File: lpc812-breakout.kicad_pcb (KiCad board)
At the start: 2 copper layers, 24 x 37.5 mm, 28 parts, among them J1 SWD, J2 Left, J3 Right, Q1 BC847BDW1, SW1 Reset, U1 LPC812M101JDH20, Y1 8MHz

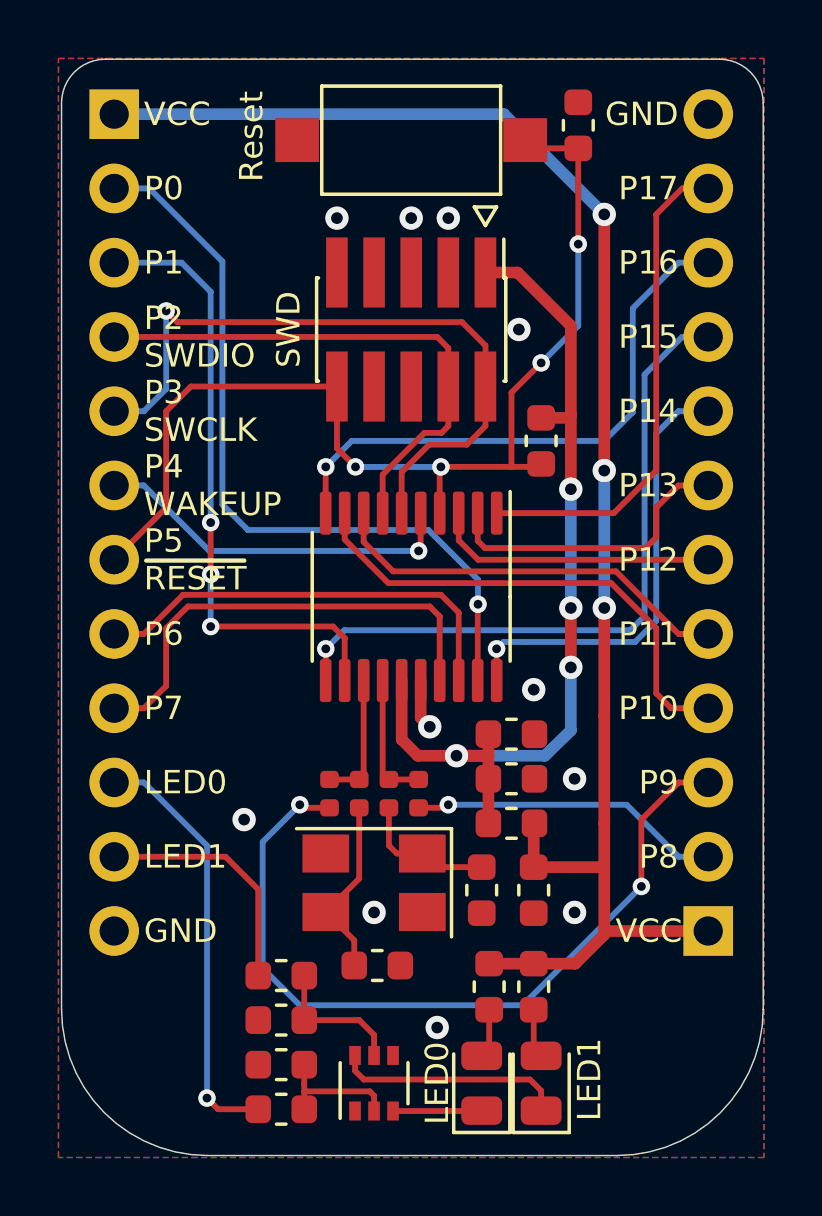
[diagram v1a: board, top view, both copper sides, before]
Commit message: Swapped SWDCLK and SWDIO - D'oh!
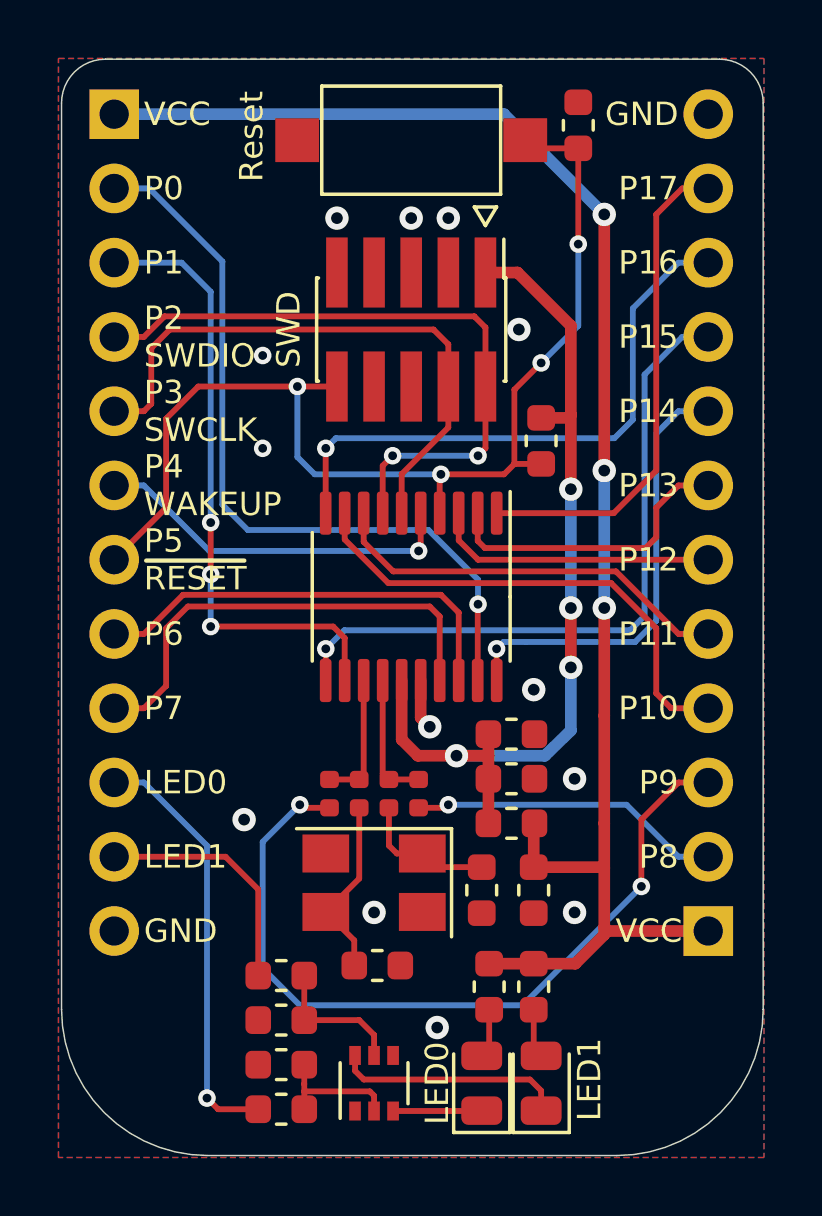
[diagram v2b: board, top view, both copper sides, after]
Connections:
- J1 pad 2: /P3_SWCLK -> /P2_SWDIO
- J1 pad 4: /P2_SWDIO -> /P3_SWCLK
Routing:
- net /P2_SWDIO: track 18.5 -> 22.7 mm, vias 0 -> 2
- net /P3_SWCLK: track 23.8 -> 20.3 mm, vias 1 -> 0
- net /~RESET: track 36.8 -> 38.0 mm
- net /P16: track 19.6 -> 20.2 mm
- net GND: vias 11 -> 13

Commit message: Swapped LED0 with LED1 on the PCB (wrong labels, d'oh!)
Rerouted the Reset and SWD tracks
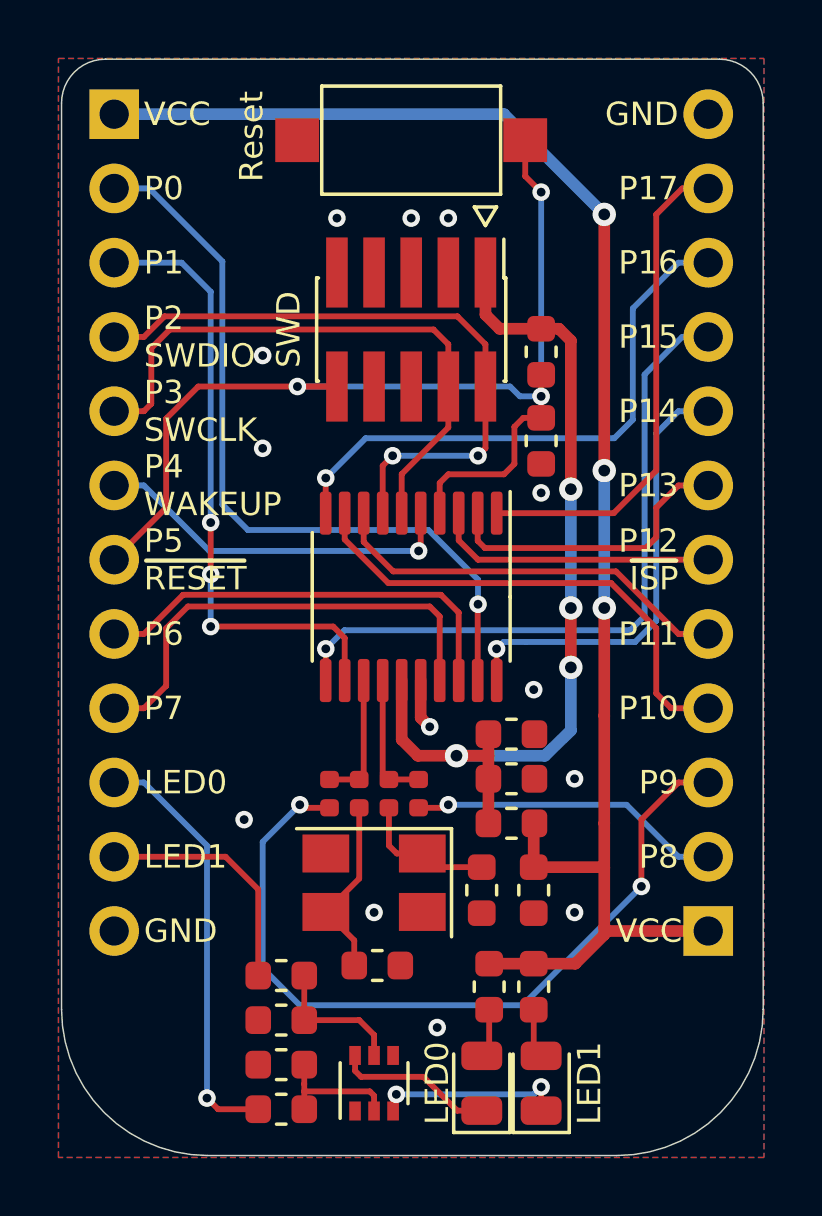
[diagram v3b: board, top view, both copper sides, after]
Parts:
- moved C5 10.9 mm to (141.6, 92.5), turned to 270 degrees
- moved R11 3.05 mm to (141.6, 89.4)
- moved D1 2.03 mm to (139.6, 114.4)
- moved D2 2.03 mm to (141.6, 114.4)
- moved R10 1.52 mm to (141.4, 111.1)
- moved R7 1.52 mm to (139.8, 111.1)
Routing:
- net Net-(D2-Pad1): track 3.04 -> 6.48 mm, vias 0 -> 2
- net Net-(D1-Pad1): track 7.85 -> 5.42 mm
- net /~RESET: track 38.0 -> 37.0 mm, vias 4 -> 3
- net /P16: track 20.2 -> 19.6 mm
- net VDD: track 31.1 -> 30.6 mm
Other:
- net class Ground added: clearance 0.2, trace_width 0.4, via_dia 0.6, via_drill 0.3
- board text added: "P12 ~ISP"
- board text removed: "P12"
